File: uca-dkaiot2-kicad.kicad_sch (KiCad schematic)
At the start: 5 parts

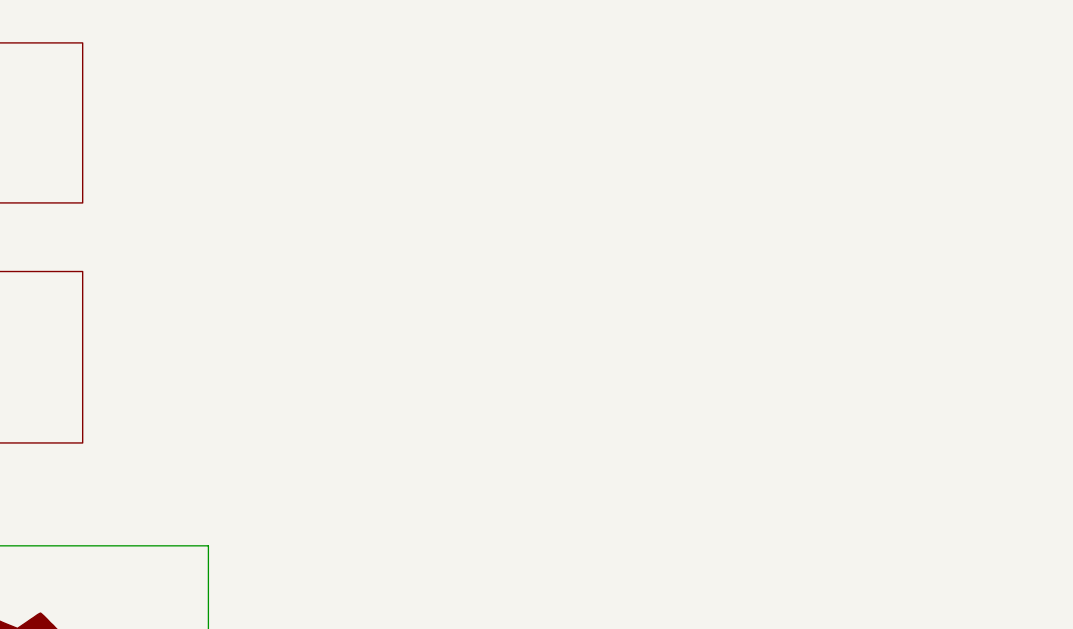
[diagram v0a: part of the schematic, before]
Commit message: WIP: import ambient-pcb-lifepo4protection and ambient-pcb-audiopower schematics
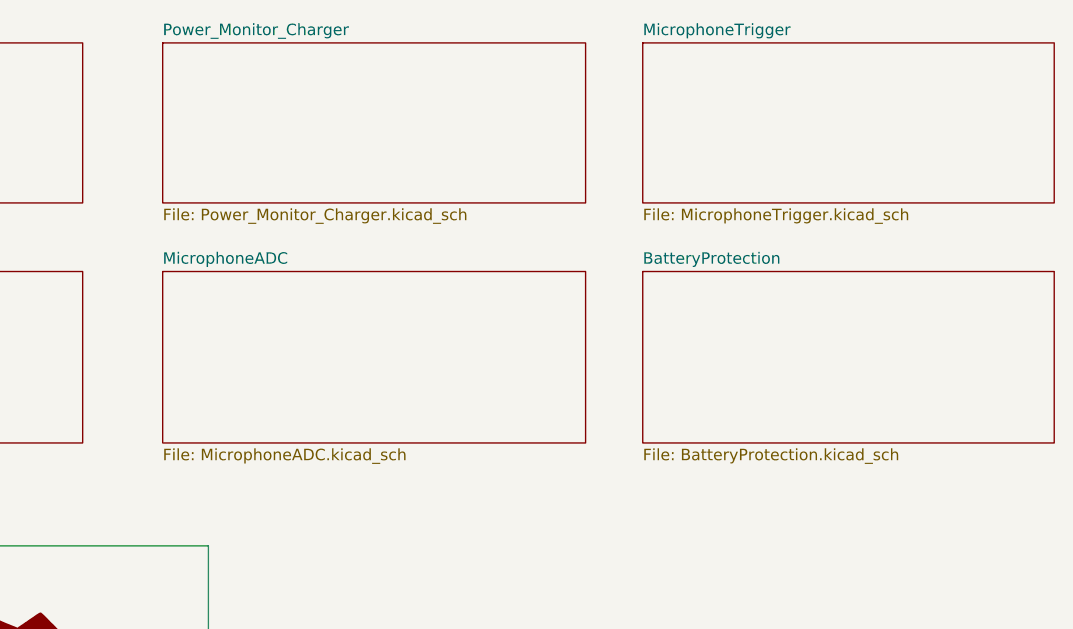
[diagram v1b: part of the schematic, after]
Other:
- added sheet BatteryProtection (BatteryProtection.kicad_sch)
- added sheet MicrophoneADC (MicrophoneADC.kicad_sch)
- added sheet MicrophoneTrigger (MicrophoneTrigger.kicad_sch)
- added sheet Power_Monitor_Charger (Power_Monitor_Charger.kicad_sch)
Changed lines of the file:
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@@
+	)
+	(sheet
+		(at 177.8 97.79)
+		(size 46.99 19.05)
+		(exclude_from_sim no)
+		(in_bom yes)
+		(on_board yes)
+		(dnp no)
+		(fields_autoplaced yes)
+		(stroke
+			(width 0.1524)
+			(type solid)
+		)
+		(fill
+			(color 0 0 0 0)
+		)
+		(property "Sheetname" "MicrophoneADC"
+			(at 177.8 97.0784 0)
+			(show_name no)
+			(do_not_autoplace no)
+			(effects
+				(font
+					(size 1.27 1.27)
+				)
+				(justify left bottom)
+			)
+		)
+		(property "Sheetfile" "MicrophoneADC.kicad_sch"
+			(at 177.8 117.4246 0)
+			(show_name no)
+			(do_not_autoplace no)
+			(effects
+				(font
+					(size 1.27 1.27)
+				)
+				(justify left top)
+			)
+		)
+		(instances
+			(project "uca-dkaiot2-kicad"
+				(path "/13b7de53-ecff-4b32-b513-b5b471d022a3"
+					(page "9")
+				)
+			)
+		)
+	)
+	(sheet
+		(at 231.14 72.39)
+		(size 45.72 17.78)
+		(exclude_from_sim no)
+		(in_bom yes)
+		(on_board yes)
+		(dnp no)
+		(fields_autoplaced yes)
+		(stroke
+			(width 0.1524)
+			(type solid)
+		)
+		(fill
+			(color 0 0 0 0)
+		)
+		(property "Sheetname" "MicrophoneTrigger"
+			(at 231.14 71.6784 0)
+			(show_name no)
+			(do_not_autoplace no)
+			(effects
+				(font
+					(size 1.27 1.27)
+				)
+				(justify left bottom)
+			)
+		)
+		(property "Sheetfile" "MicrophoneTrigger.kicad_sch"
+			(at 231.14 90.7546 0)
+			(show_name no)
+			(do_not_autoplace no)
+			(effects
+				(font
+					(size 1.27 1.27)
+				)
+				(justify left top)
+			)
+		)
+		(instances
+			(project "uca-dkaiot2-kicad"
+				(path "/13b7de53-ecff-4b32-b513-b5b471d022a3"
+					(page "10")
+				)
+			)
+		)
+	)
+	(sheet
+		(at 177.8 72.39)
+		(size 46.99 17.78)
+		(exclude_from_sim no)
+		(in_bom yes)
+		(on_board yes)
+		(dnp no)
+		(fields_autoplaced yes)
+		(stroke
+			(width 0.1524)
+			(type solid)
+		)
+		(fill
+			(color 0 0 0 0)
+		)
+		(property "Sheetname" "Power_Monitor_Charger"
+			(at 177.8 71.6784 0)
+			(show_name no)
+			(do_not_autoplace no)
+			(effects
+				(font
+					(size 1.27 1.27)
+				)
+				(justify left bottom)
+			)
+		)
+		(property "Sheetfile" "Power_Monitor_Charger.kicad_sch"
+			(at 177.8 90.7546 0)
+			(show_name no)
+			(do_not_autoplace no)
+			(effects
+				(font
+					(size 1.27 1.27)
+				)
+				(justify left top)
+			)
+		)
+		(instances
+			(project "uca-dkaiot2-kicad"
+				(path "/13b7de53-ecff-4b32-b513-b5b471d022a3"
+					(page "8")
+				)
+			)
+		)
 	)
 	(sheet
@@
 				)
 			)
+		)
+	)
+	(sheet
+		(at 231.14 97.79)
+		(size 45.72 19.05)
+		(exclude_from_sim no)
+		(in_bom yes)
+		(on_board yes)
+		(dnp no)
+		(fields_autoplaced yes)
+		(stroke
+			(width 0.1524)
+			(type solid)
+		)
+		(fill
+			(color 0 0 0 0)
+		)
+		(property "Sheetname" "BatteryProtection"
+			(at 231.14 97.0784 0)
+			(show_name no)
+			(do_not_autoplace no)
+			(effects
+				(font
+					(size 1.27 1.27)
+				)
+				(justify left bottom)
+			)
+		)
+		(property "Sheetfile" "BatteryProtection.kicad_sch"
+			(at 231.14 117.4246 0)
+			(show_name no)
+			(do_not_autoplace no)
+			(effects
+				(font
+					(size 1.27 1.27)
+				)
+				(justify left top)
+			)
+		)
+		(instances
+			(project "uca-dkaiot2-kicad"
+				(path "/13b7de53-ecff-4b32-b513-b5b471d022a3"
+					(page "11")
+				)
+			)
